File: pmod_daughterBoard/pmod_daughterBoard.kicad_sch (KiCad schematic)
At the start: 14 parts, among them J1 Conn_02x06_Odd_Even, J2 Conn_Coaxial, J3 Conn_02x09_Odd_Even, Q1 N/A

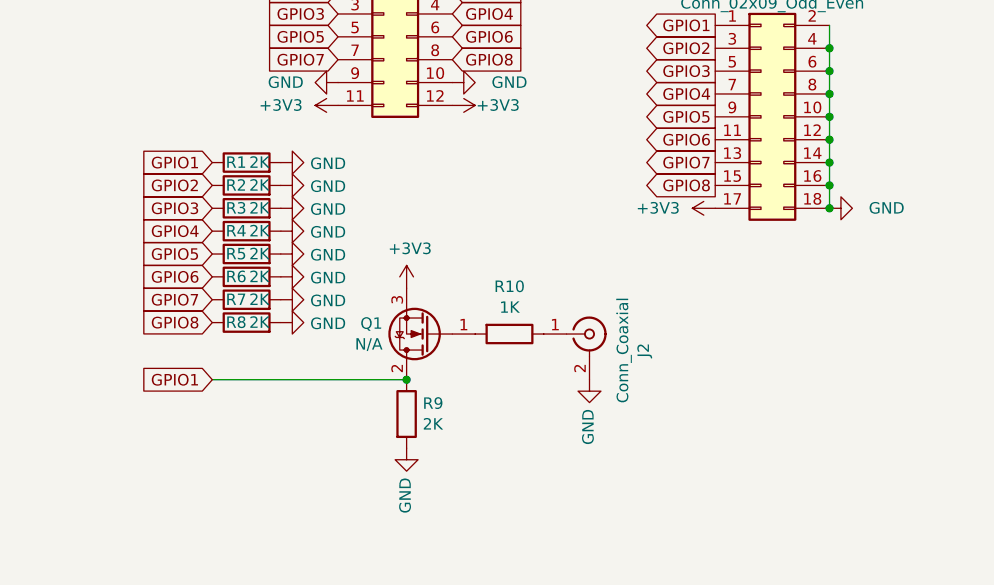
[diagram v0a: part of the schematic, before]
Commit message: began implementation of various gpio inputs. Removed redundant GND resistor
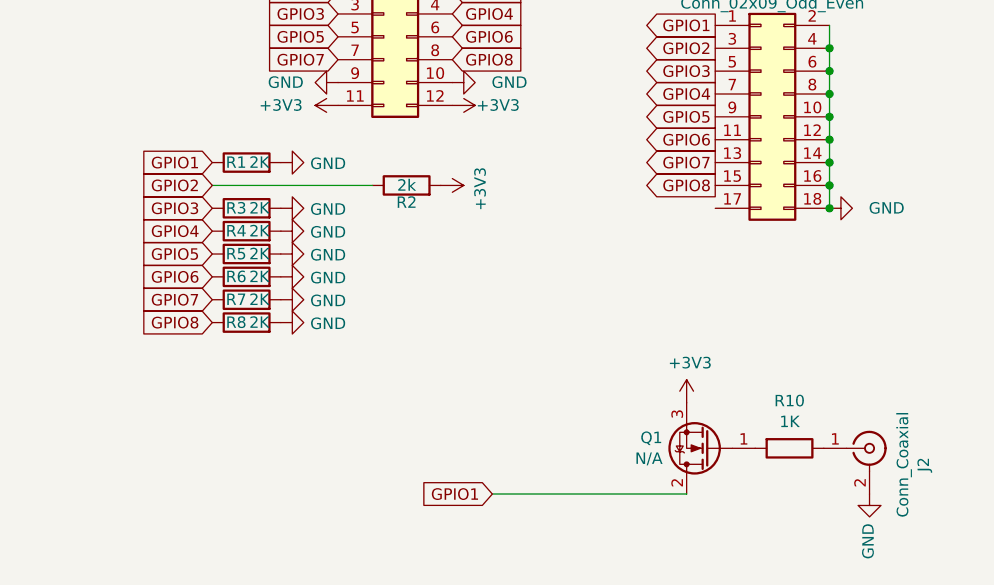
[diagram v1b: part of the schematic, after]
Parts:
- removed R9: 2K, Resistor_SMD:R_0402_1005Metric, symbol Device:R
- R2: value 2K -> 2k; Link https://www.mouser.com/ProductDetail/YAGEO/AC0402JR-072KL?q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 -> (none); Part Number 603-AC0402JR-072KL -> (none)
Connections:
- net +3V3: now also R2.2; no longer J3.17 (Pin_17)
- net GND: no longer R2.2
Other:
- moved on the sheet: J2, Q1, R10

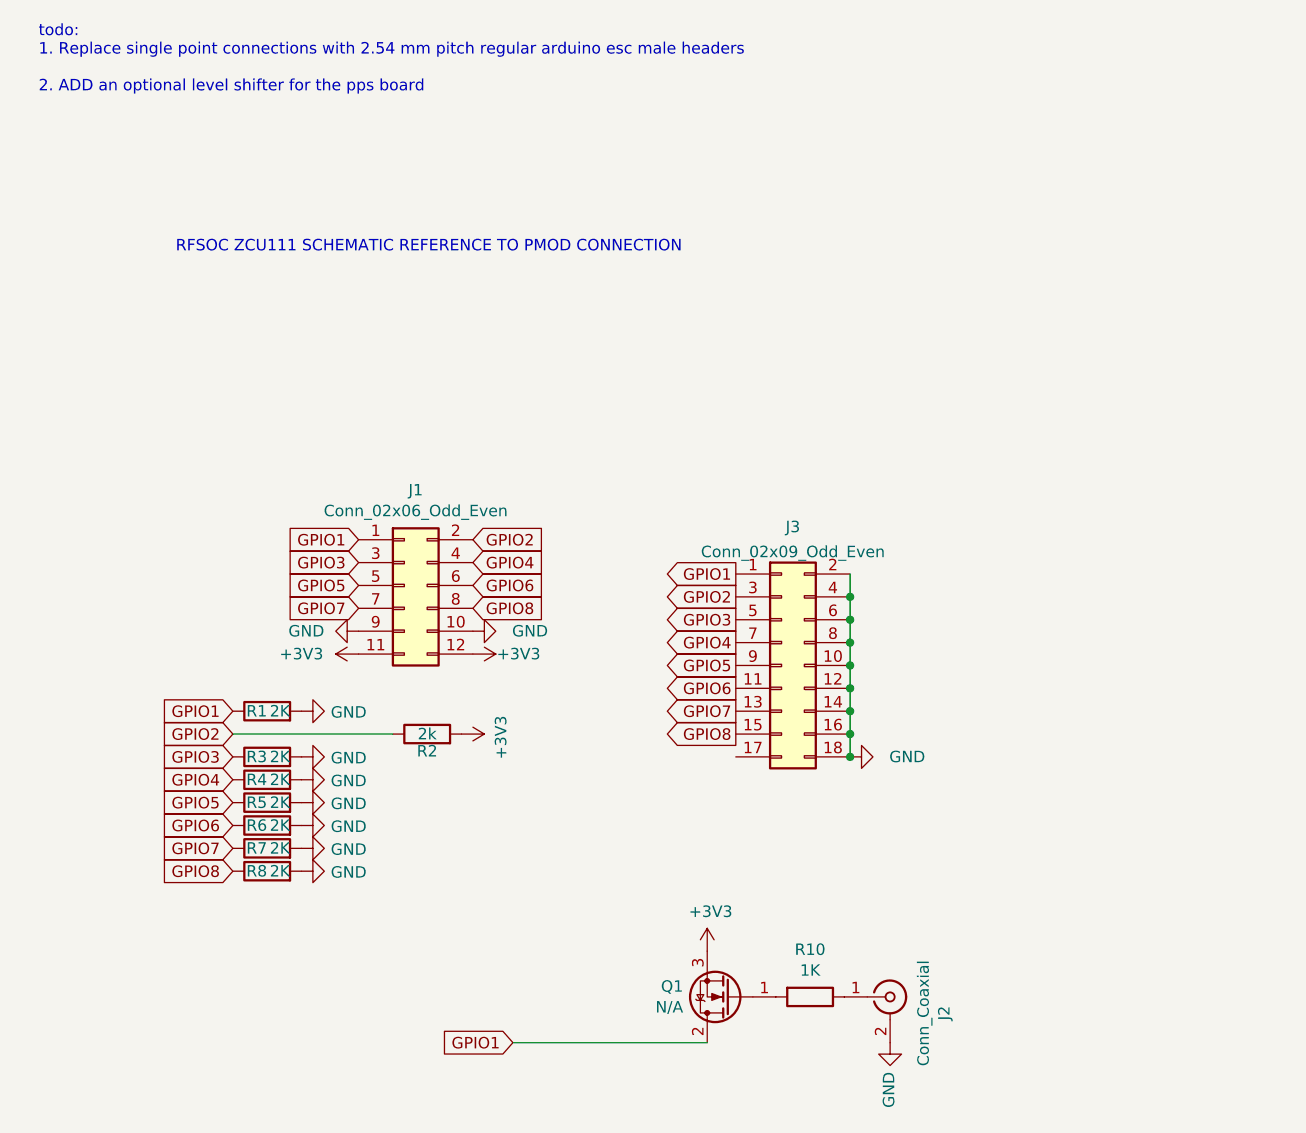
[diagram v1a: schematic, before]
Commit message: implemented differential pair receiver on pmod board
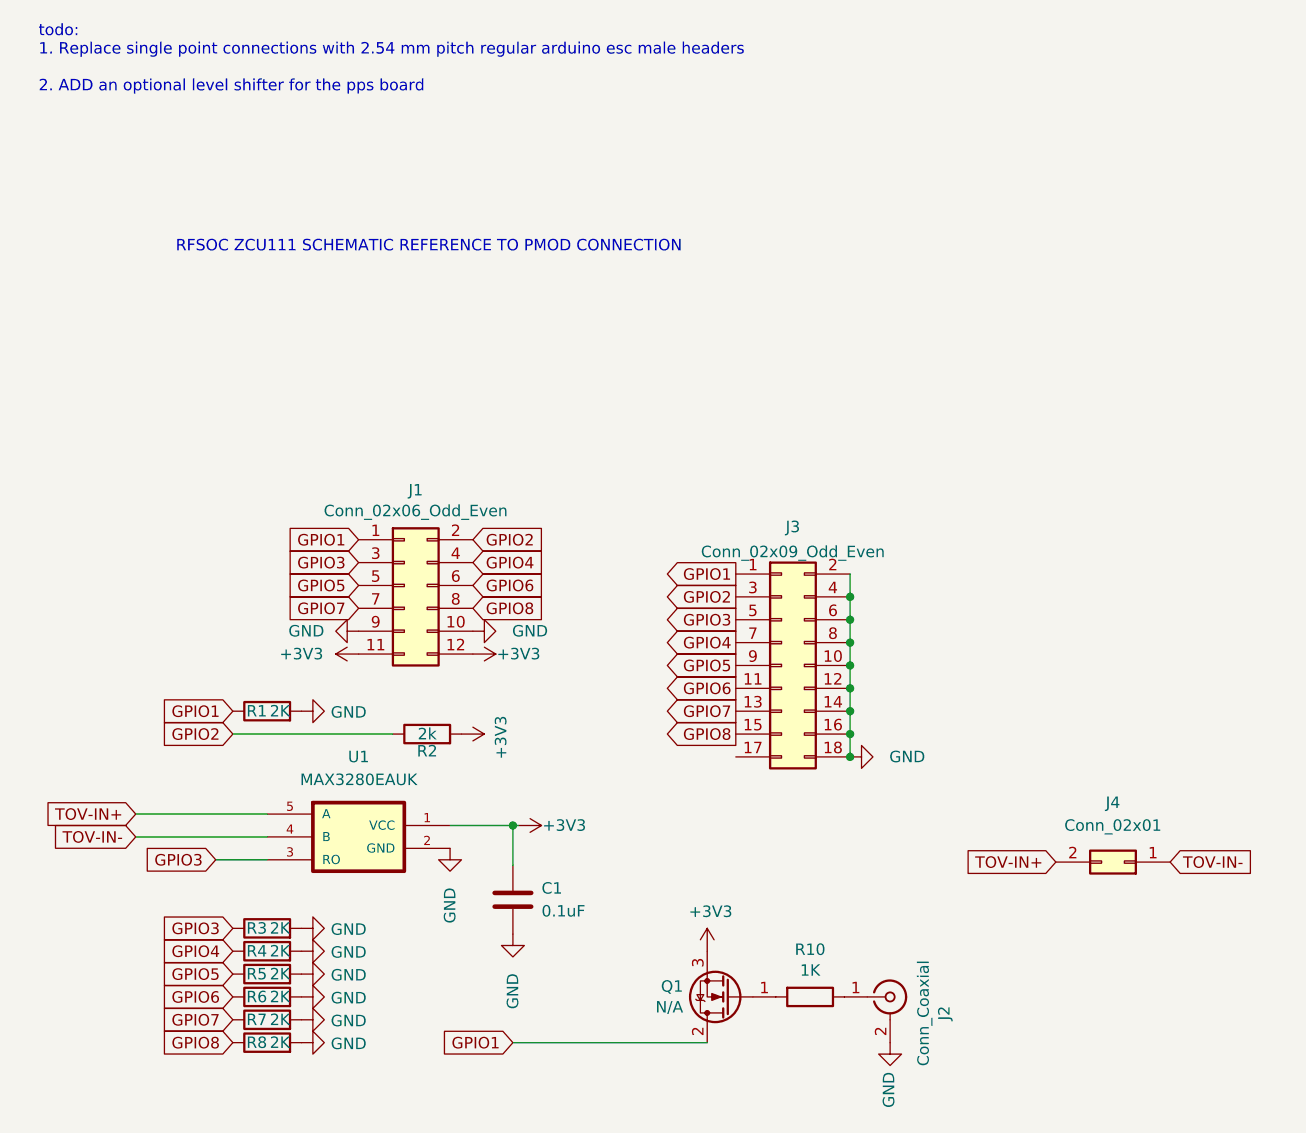
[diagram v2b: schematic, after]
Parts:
- added C1: 0.1uF, Capacitor_SMD:C_0402_1005Metric, symbol Device:C
- added J4: Conn_02x01, Connector_PinHeader_2.54mm:PinHeader_2x01_P2.54mm_Vertical, symbol Connector_Generic:Conn_02x01
- added U1: MAX3280EAUK, SOT95P280X145-5N, symbol max3280:MAX3280EAUK
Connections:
- net +3V3: now also C1.2, U1.1 (VCC)
- net GND: now also C1.1, U1.2 (GND)
- net GPIO3: now also U1.3 (RO)
- new net TOV-IN+: J4.2 (Pin_2), U1.5 (A)
- new net TOV-IN-: J4.1 (Pin_1), U1.4 (B)
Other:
- moved on the sheet: R4, R5, R6, R7, R8

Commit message: updated
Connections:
- net +3V3: now also J3.17 (Pin_17)
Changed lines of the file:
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@@
     (pin "2")
+  )
+  (symbol (lib_id "power:+3V3") (at 186.69 172.72 90) (unit 1)
+    (in_bom yes) (on_board yes)
+    (property "Reference" "#PWR?" (id 0) (at 190.5 172.72 0)
+      (effects (font (size 1.27 1.27)) hide)
+    )
+    (property "Value" "+3V3" (id 1) (at 181.61 172.72 90))
+    (property "Footprint" "" (id 2) (at 186.69 172.72 0)
+      (effects (font (size 1.27 1.27)) hide)
+    )
+    (property "Datasheet" "" (id 3) (at 186.69 172.72 0)
+      (effects (font (size 1.27 1.27)) hide)
+    )
+    (pin "1")
   )
   (symbol (lib_id "Device:R") (at 152.4 170.18 90) (unit 1)
@@
       (reference "#PWR0101") (unit 1) (value "+3V3") (footprint "")
     )
+    (path "/44b016cf-8ac1-4430-b5be-c8ecfe9e9d06"
+      (reference "#PWR?") (unit 1) (value "+3V3") (footprint "")
+    )
     (path "/a52bbc9b-d893-4f4a-83b5-2563eb31e455"
